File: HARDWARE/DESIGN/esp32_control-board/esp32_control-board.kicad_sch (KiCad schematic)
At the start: 0 parts

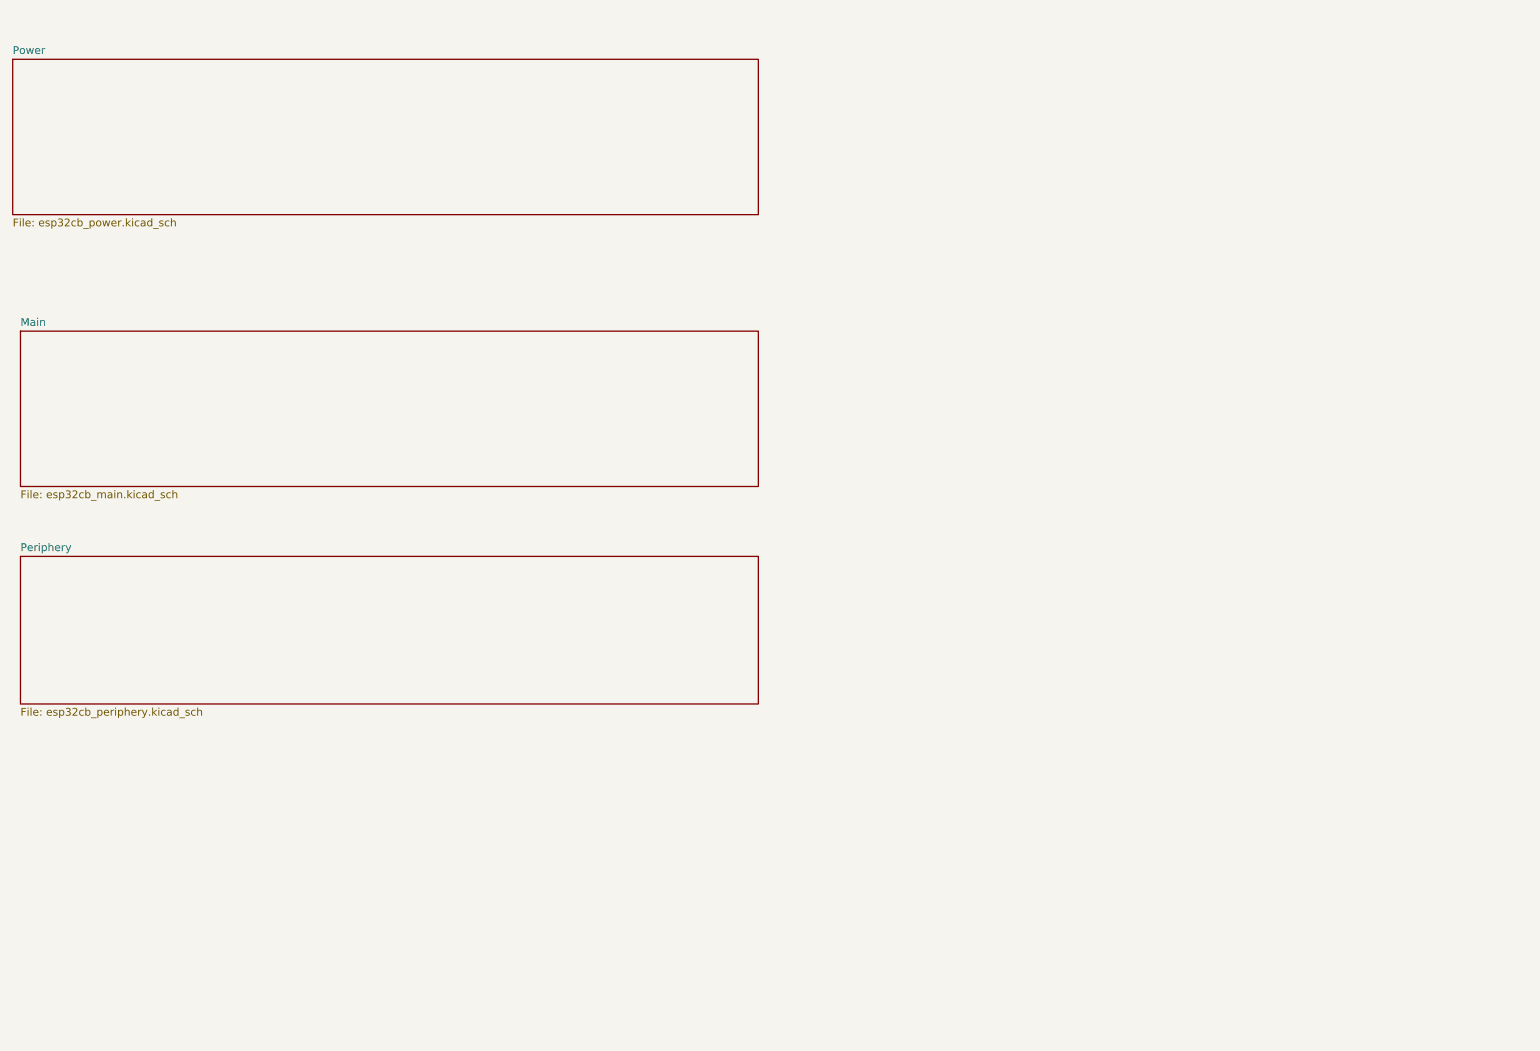
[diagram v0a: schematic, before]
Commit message: 60707 - schematics and readme updated, preliminary PCB-layout prepared
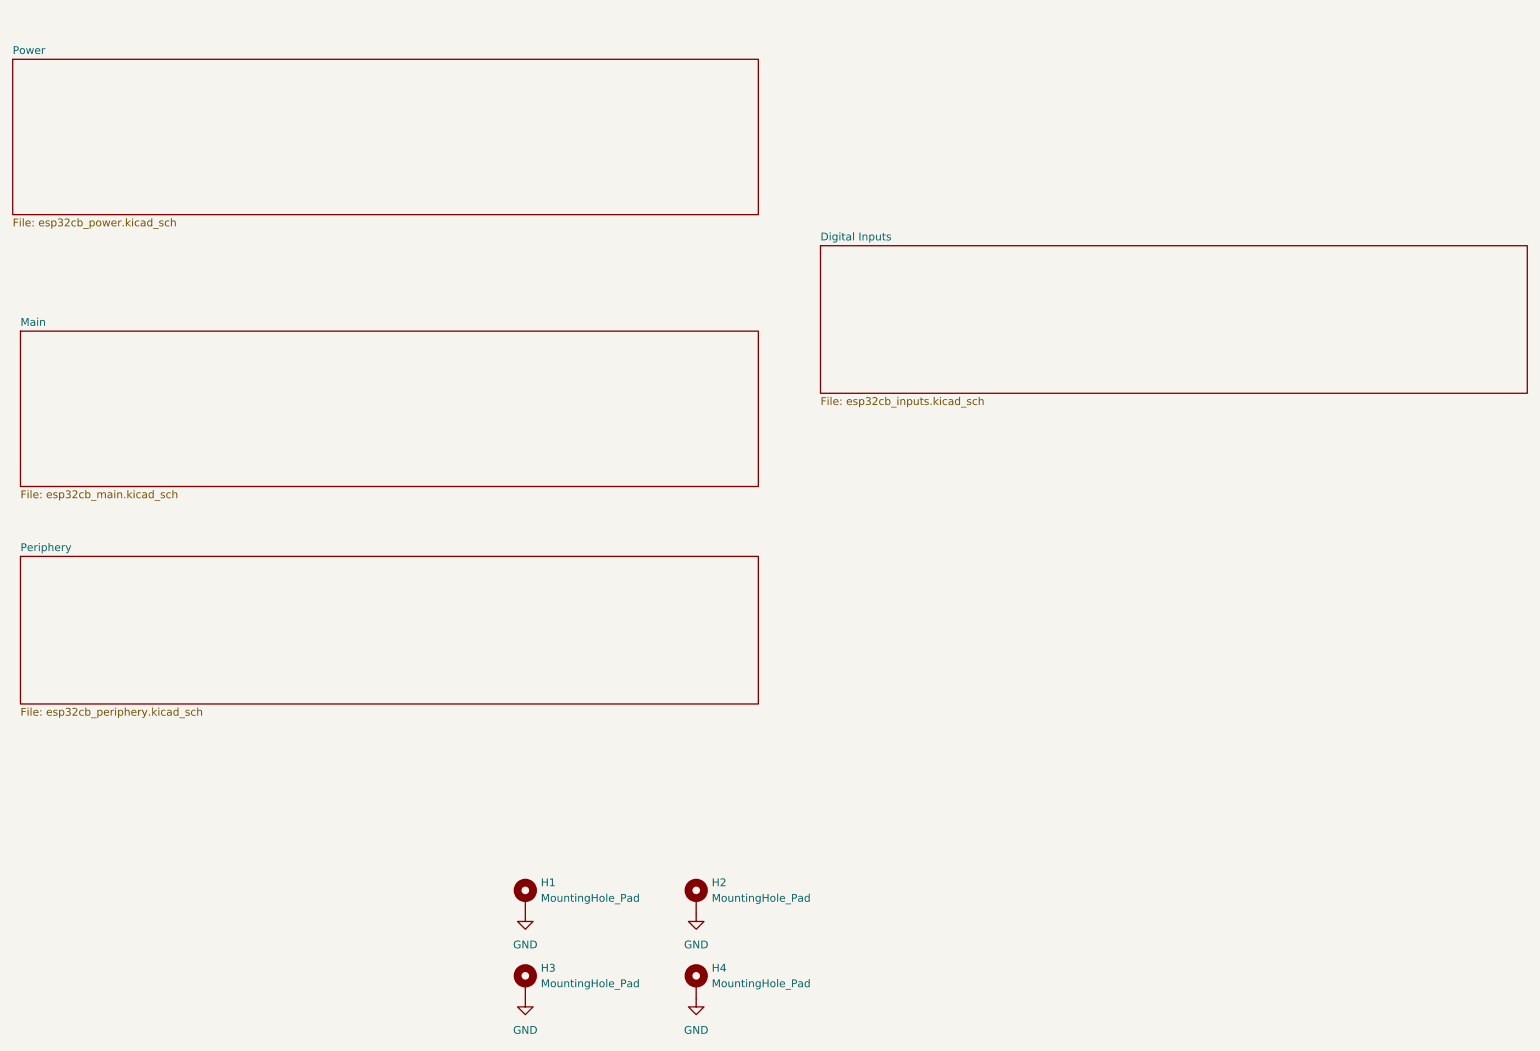
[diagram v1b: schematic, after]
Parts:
- added H1, H2, H3, H4: MountingHole_Pad, MountingHole:MountingHole_3.2mm_M3_DIN965_Pad_TopBottom, symbol Mechanical:MountingHole_Pad
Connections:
- new net GND: H1.1, H2.1, H3.1, H4.1
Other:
- added sheet Digital Inputs (esp32cb_inputs.kicad_sch)
- title: (none) -> ESP32-based Control Board

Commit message: 60710 - schematic and PCB-layout updated
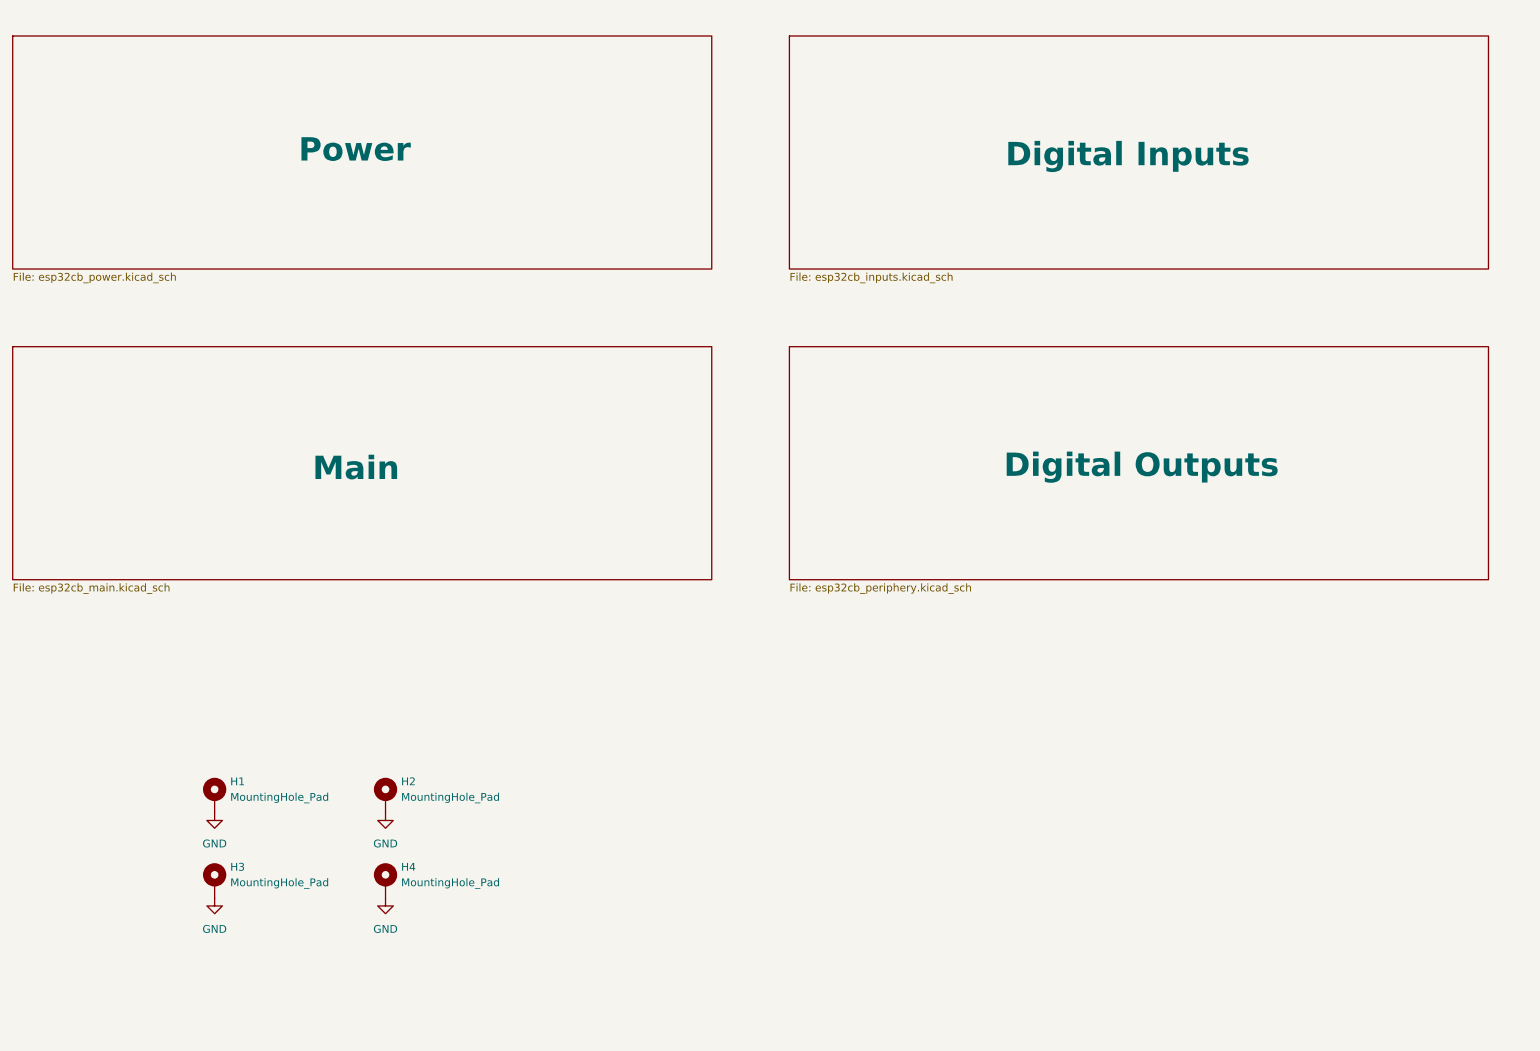
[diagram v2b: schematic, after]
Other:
- sheet Periphery renamed Digital Outputs
- moved on the sheet: H1, H2, H3, H4

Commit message: 60821 - Schematic is under reconstruction for ver.2
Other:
- removed sheet Digital Inputs
- removed sheet Digital Outputs
- added sheet Locks (esp32cb_locks.kicad_sch)
- added sheet Peripherals (esp32cb_peripheral.kicad_sch)
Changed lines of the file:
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@@
 	(title_block
 		(title "ESP32-based Control Board")
-		(date "2026-07-14")
-		(rev "1a")
+		(date "2026-08-21")
+		(rev "2a")
 	)
 	(symbol
@@
 	)
 	(sheet
-		(at 152.4 25.4)
+		(at 152.4 76.2)
 		(size 114.3 38.1)
 		(exclude_from_sim no)
@@
 		)
 		(fill
-			(color 204 255 204 1)
-		)
-		(property "Sheetname" "Digital Inputs"
-			(at 187.706 46.99 0)
+			(color 255 255 194 1)
+		)
+		(property "Sheetname" "Peripherals"
+			(at 192.786 97.282 0)
 			(show_name no)
 			(do_not_autoplace no)
@@
 			)
 		)
-		(property "Sheetfile" "esp32cb_inputs.kicad_sch"
-			(at 152.4 64.0846 0)
+		(property "Sheetfile" "esp32cb_peripheral.kicad_sch"
+			(at 152.4 114.8846 0)
 			(show_name no)
 			(do_not_autoplace no)
@@
 			(project "esp32_control-board"
 				(path "/71812bfc-9597-4f26-a67f-4f6ff697416c"
-					(page "4")
+					(page "6")
 				)
 			)
@@
 	)
 	(sheet
-		(at 152.4 76.2)
+		(at 25.4 76.2)
 		(size 114.3 38.1)
 		(exclude_from_sim no)
@@
 		)
 		(fill
-			(color 179 230 255 1)
-		)
-		(property "Sheetname" "Digital Outputs"
-			(at 187.452 97.79 0)
+			(color 194 194 194 1)
+		)
+		(property "Sheetname" "Locks"
+			(at 73.406 97.536 0)
 			(show_name no)
 			(do_not_autoplace no)
@@
 			)
 		)
-		(property "Sheetfile" "esp32cb_periphery.kicad_sch"
-			(at 152.4 114.8846 0)
+		(property "Sheetfile" "esp32cb_locks.kicad_sch"
+			(at 25.4 114.8846 0)
 			(show_name no)
 			(do_not_autoplace no)
@@
 			(project "esp32_control-board"
 				(path "/71812bfc-9597-4f26-a67f-4f6ff697416c"
-					(page "3")
+					(page "5")
 				)
 			)
@@
 	)
 	(sheet
-		(at 25.4 76.2)
+		(at 152.4 25.4)
 		(size 114.3 38.1)
 		(exclude_from_sim no)
@@
 		)
 		(property "Sheetname" "Main"
-			(at 74.422 98.298 0)
+			(at 201.422 47.498 0)
 			(show_name no)
 			(do_not_autoplace no)
@@
 		)
 		(property "Sheetfile" "esp32cb_main.kicad_sch"
-			(at 25.4 114.8846 0)
-			(show_name no)
-			(do_not_autoplace no)
+			(at 152.4 64.0846 0)
+			(show_name no)
+			(do_not_autoplace no)

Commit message: 60825 - Schematic update and PCB-layout started
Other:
- added sheet CAN-interface (esp32cb_can.kicad_sch)
- moved on the sheet: H1, H2, H3, H4
